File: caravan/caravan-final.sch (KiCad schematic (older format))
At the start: 49 parts

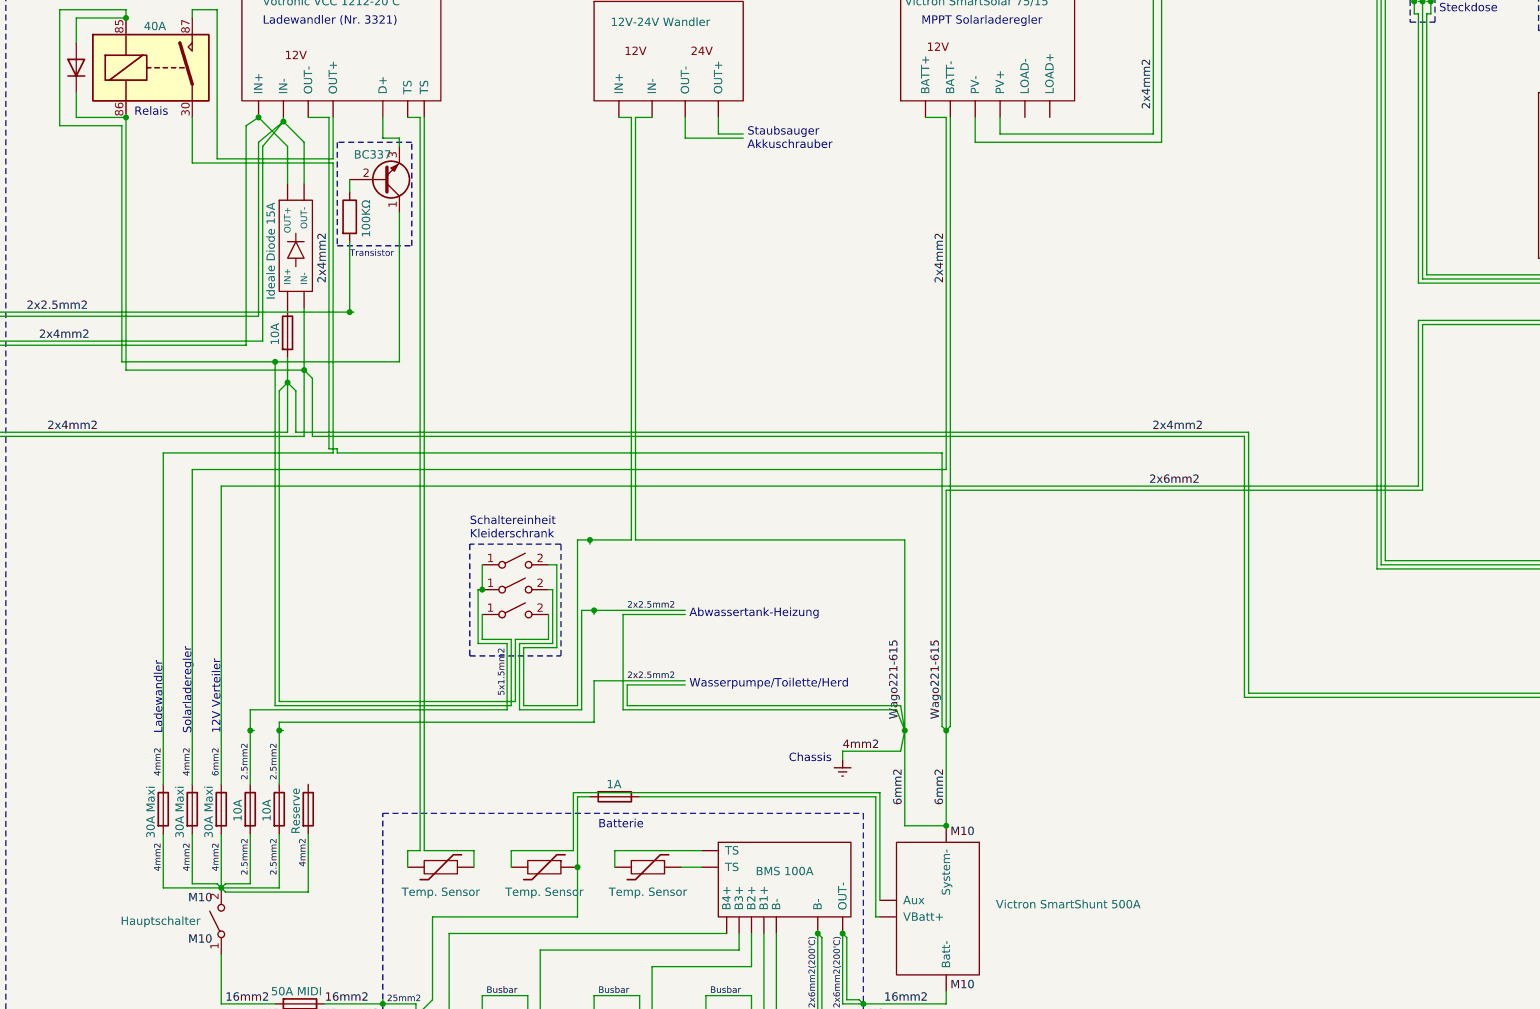
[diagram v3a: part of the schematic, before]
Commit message: caravan: Use standard fuse for Victron MPPT.          Reserve Maxi fuse for future use.
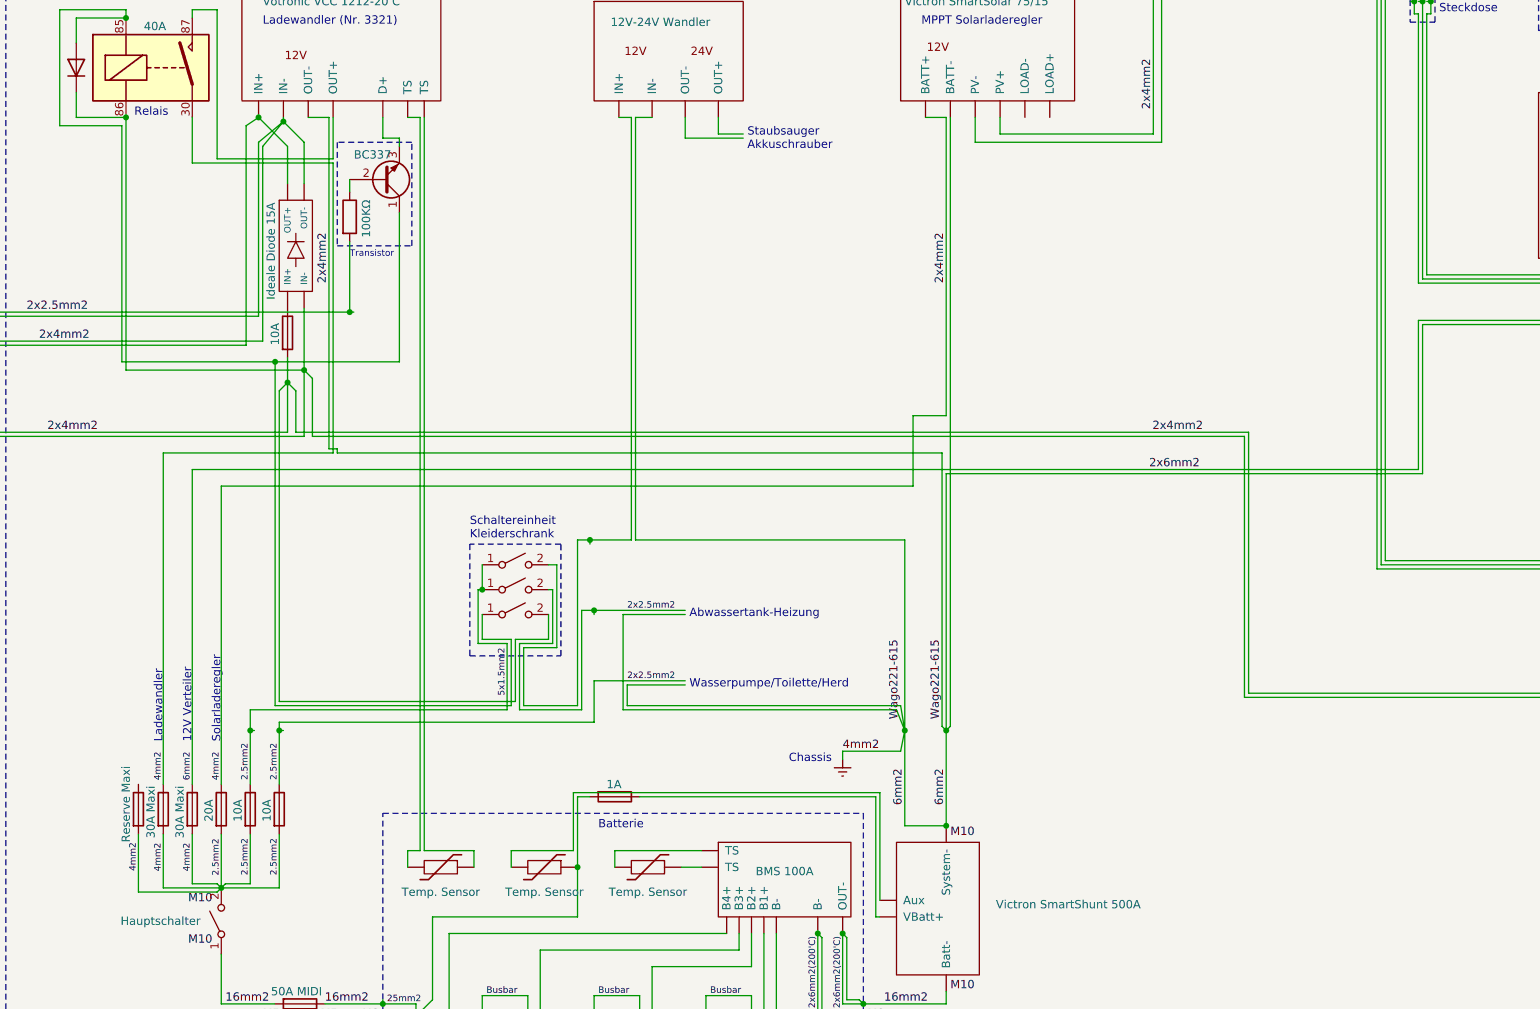
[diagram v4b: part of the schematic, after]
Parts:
- F?: value 30A Maxi -> 20A
- F?: value Reserve -> Reserve Maxi
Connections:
- wire segments 421 -> 423
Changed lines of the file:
@@
 	11200 6575 12525 6575
 Wire Wire Line
-	8550 6150 11425 6150
-Wire Wire Line
-	11425 6150 11425 5150
-Wire Wire Line
-	11400 6125 11400 5125
+	11400 6025 11400 5125
 $Comp
 L power:Earth #PWR?
@@
 L Device:Fuse F?
 U 1 1 6048F6FE
-P 4175 8075
-F 0 "F?" H 4235 8121 50  0001 L CNN
-F 1 "30A Maxi" V 4100 7900 50  0000 L CNN
-F 2 "" V 4105 8075 50  0001 C CNN
-F 3 "~" H 4175 8075 50  0001 C CNN
-	1    4175 8075
-	1    0    0    -1
-$EndComp
-Wire Wire Line
-	8550 6150 8550 7600
+P 4000 8075
+F 0 "F?" H 4060 8121 50  0001 L CNN
+F 1 "30A Maxi" V 3925 7900 50  0000 L CNN
+F 2 "" V 3930 8075 50  0001 C CNN
+F 3 "~" H 4000 8075 50  0001 C CNN
+	1    4000 8075
+	1    0    0    -1
+$EndComp
 Wire Wire Line
 	8525 7575 8550 7600
@@
 Text Label 5775 9200 0    39   ~ 0
 Busbar
-Text Label 4175 8450 1    39   ~ 0
-4mm2
-Text Label 4175 7875 1    39   ~ 0
+Text Label 4175 8475 1    39   ~ 0
+2.5mm2
+Text Label 4000 7900 1    39   ~ 0
 6mm2
 Text Label 8525 7050 3    50   ~ 0
@@
 	9850 4050 8725 4050
 Wire Wire Line
-	4175 8225 4175 8550
-Wire Wire Line
 	4200 8525 4175 8550
 Text Label 4350 8250 3    39   ~ 0
@@
 Connection ~ 4175 8550
 Wire Wire Line
-	4175 8550 4200 8575
+	4175 8550 4150 8575
 Wire Wire Line
 	4200 8525 4350 8525
@@
 Wire Wire Line
 	8300 8175 8300 7600
-Text Label 9775 6125 0    50   ~ 0
+Text Label 9775 6025 0    50   ~ 0
 2x6mm2
 $Comp
@@
 	8575 3900 8575 7575
 Wire Wire Line
-	8550 3900 8550 6025
-Wire Wire Line
 	6650 3900 6650 6450
 Wire Wire Line
@@
 L Device:Fuse F?
 U 1 1 626DA299
-P 4000 8075
-F 0 "F?" H 4060 8121 50  0001 L CNN
-F 1 "30A Maxi" V 3925 7900 50  0000 L CNN
-F 2 "" V 3930 8075 50  0001 C CNN
-F 3 "~" H 4000 8075 50  0001 C CNN
-	1    4000 8075
+P 4175 8075
+F 0 "F?" H 4235 8121 50  0001 L CNN
+F 1 "20A" V 4100 8000 50  0000 L CNN
+F 2 "" V 4105 8075 50  0001 C CNN
+F 3 "~" H 4175 8075 50  0001 C CNN
+	1    4175 8075
 	1    0    0    -1
 $EndComp
@@
 	3825 8550 3825 8225
 Wire Wire Line
-	4000 8225 4000 8525
-Wire Wire Line
-	4000 8525 4150 8525
-Wire Wire Line
-	4175 8550 4150 8525
-Wire Wire Line
 	3825 8550 4175 8550
 Wire Wire Line
-	4000 6025 8550 6025
-Wire Wire Line
-	4000 6025 4000 7925
-Wire Wire Line
 	3825 7925 3825 5925
 Wire Wire Line
 	3825 5925 4850 5925
-Wire Wire Line
-	4175 6125 11400 6125
 Wire Wire Line
 	4825 5900 4875 5900
@@
 Text Label 3825 8450 1    39   ~ 0
 4mm2
-Text Label 4000 7875 1    39   ~ 0
+Text Label 4175 7900 1    39   ~ 0
 4mm2
-Text Label 3825 7875 1    39   ~ 0
+Text Label 3825 7900 1    39   ~ 0
 4mm2
+Wire Wire Line
+	3675 8575 3675 8225
+Wire Wire Line
+	4175 8550 4525 8550
+Wire Wire Line
+	4525 8550 4525 8225
+Text Label 3675 8275 3    39   ~ 0
+4mm2
+Wire Wire Line
+	4000 6025 4000 7925
+Wire Wire Line
+	4175 8225 4175 8550
+Wire Wire Line
+	4175 6125 4175 7925
+Wire Wire Line
+	4175 6125 8350 6125
+Wire Wire Line
+	4000 6025 11400 6025
+Wire Wire Line
+	8550 6050 11425 6050
+Wire Wire Line
+	11425 6050 11425 5150
+Wire Wire Line
+	8550 6050 8550 7600
+Wire Wire Line
+	8350 6125 8350 5700
+Wire Wire Line
+	8350 5700 8550 5700
+Wire Wire Line
+	8550 5700 8550 3900
+Wire Wire Line
+	4000 8225 4000 8525
+Wire Wire Line
+	4000 8525 4150 8525
+Wire Wire Line
+	4150 8525 4175 8550
+Wire Wire Line
+	4150 8575 3675 8575
+Text Notes 3825 7675 1    50   ~ 0
+Ladewandler
+Text Notes 4175 7675 1    50   ~ 0
+Solarladeregler
+Text Notes 4000 7675 1    50   ~ 0
+12V Verteiler
 $Comp
 L Device:Fuse F?
 U 1 1 62BF37F1
-P 4700 8075
-F 0 "F?" H 4760 8121 50  0001 L CNN
-F 1 "Reserve" V 4625 7925 50  0000 L CNN
-F 2 "" V 4630 8075 50  0001 C CNN
-F 3 "~" H 4700 8075 50  0001 C CNN
-	1    4700 8075
-	1    0    0    -1
-$EndComp
-Wire Wire Line
-	4200 8575 4700 8575
-Wire Wire Line
-	4700 8575 4700 8225
-Wire Wire Line
-	4175 8550 4525 8550
-Wire Wire Line
-	4525 8550 4525 8225
-Text Label 4700 8250 3    39   ~ 0
-4mm2
-Wire Wire Line
-	4175 6125 4175 7925
-Text Notes 3825 7625 1    50   ~ 0
-Ladewandler
-Text Notes 4000 7625 1    50   ~ 0
-Solarladeregler
-Text Notes 4175 7625 1    50   ~ 0
-12V Verteiler
+P 3675 8075
+F 0 "F?" H 3735 8121 50  0001 L CNN
+F 1 "Reserve Maxi" V 3600 7875 50  0000 L CNN
+F 2 "" V 3605 8075 50  0001 C CNN
+F 3 "~" H 3675 8075 50  0001 C CNN
+	1    3675 8075
+	1    0    0    -1
+$EndComp
 $EndSCHEMATC
